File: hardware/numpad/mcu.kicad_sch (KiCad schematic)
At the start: 9 parts, among them J4 Conn_01x02_Female, J5 Conn_01x02_Male, U1 STM32L011F4Px

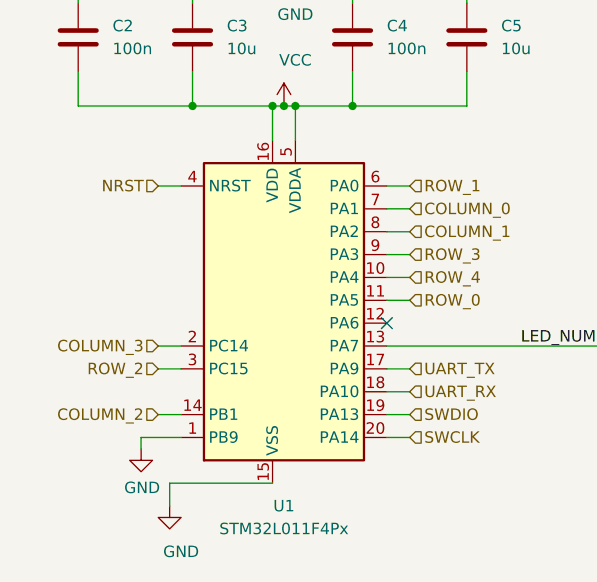
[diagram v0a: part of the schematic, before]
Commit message: Numpad: Exchange MCU for an available version
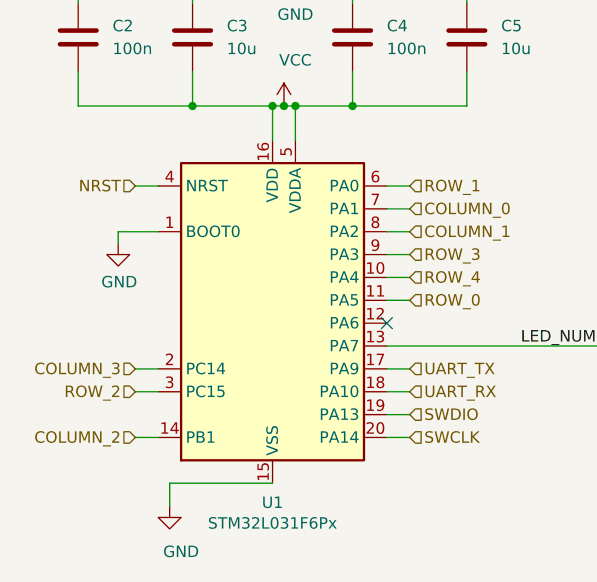
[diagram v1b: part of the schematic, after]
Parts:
- removed U1: STM32L011F4Px, Package_SO:TSSOP-20_4.4x6.5mm_P0.65mm, symbol MCU_ST_STM32L0:STM32L011F4Px
- added U1: STM32L031F6Px, Package_SO:TSSOP-20_4.4x6.5mm_P0.65mm, symbol MCU_ST_STM32L0:STM32L031F6Px
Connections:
- net COLUMN_0: now also U1.7 (PA1)
- net COLUMN_1: now also U1.8 (PA2)
- net COLUMN_2: now also U1.14 (PB1)
- net COLUMN_3: now also U1.2 (PC14)
- net GND: now also U1.1 (BOOT0), U1.15 (VSS)
- net LED_NUMLOCK: now also U1.13 (PA7)
- net NRST: now also U1.4 (NRST)
- net ROW_0: now also U1.11 (PA5)
- net ROW_1: now also U1.6 (PA0)
- net ROW_2: now also U1.3 (PC15)
- net ROW_3: now also U1.9 (PA3)
- net ROW_4: now also U1.10 (PA4)
- net SWCLK: now also U1.20 (PA14)
- net SWDIO: now also U1.19 (PA13)
- net UART_RX: now also U1.18 (PA10)
- net UART_TX: now also U1.17 (PA9)
- net VCC: now also U1.16 (VDD), U1.5 (VDDA)
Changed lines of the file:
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@@
     (stroke (width 0) (type solid) (color 0 0 0 0))
   )
-  (wire (pts (xy 86.995 118.11) (xy 91.44 118.11))
-    (stroke (width 0) (type solid) (color 0 0 0 0))
-  )
-  (wire (pts (xy 86.995 119.38) (xy 86.995 118.11))
-    (stroke (width 0) (type solid) (color 0 0 0 0))
-  )
-  (wire (pts (xy 88.9 90.17) (xy 91.44 90.17))
-    (stroke (width 0) (type solid) (color 0 0 0 0))
-  )
-  (wire (pts (xy 88.9 107.95) (xy 91.44 107.95))
-    (stroke (width 0) (type solid) (color 0 0 0 0))
-  )
-  (wire (pts (xy 88.9 110.49) (xy 91.44 110.49))
-    (stroke (width 0) (type solid) (color 0 0 0 0))
-  )
-  (wire (pts (xy 88.9 115.57) (xy 91.44 115.57))
+  (wire (pts (xy 84.455 95.25) (xy 88.9 95.25))
+    (stroke (width 0) (type solid) (color 0 0 0 0))
+  )
+  (wire (pts (xy 84.455 96.52) (xy 84.455 95.25))
+    (stroke (width 0) (type solid) (color 0 0 0 0))
+  )
+  (wire (pts (xy 86.36 90.17) (xy 88.9 90.17))
+    (stroke (width 0) (type solid) (color 0 0 0 0))
+  )
+  (wire (pts (xy 86.36 110.49) (xy 88.9 110.49))
+    (stroke (width 0) (type solid) (color 0 0 0 0))
+  )
+  (wire (pts (xy 86.36 113.03) (xy 88.9 113.03))
+    (stroke (width 0) (type solid) (color 0 0 0 0))
+  )
+  (wire (pts (xy 86.36 118.11) (xy 88.9 118.11))
     (stroke (width 0) (type solid) (color 0 0 0 0))
   )
@@
     (effects (font (size 1.27 1.27)) (justify left bottom))
   )
-  (hierarchical_label "NRST" (shape input) (at 88.9 90.17 180)
+  (hierarchical_label "NRST" (shape input) (at 86.36 90.17 180)
     (effects (font (size 1.27 1.27)) (justify right))
   )
-  (hierarchical_label "COLUMN_3" (shape input) (at 88.9 107.95 180)
+  (hierarchical_label "COLUMN_3" (shape input) (at 86.36 110.49 180)
     (effects (font (size 1.27 1.27)) (justify right))
   )
-  (hierarchical_label "ROW_2" (shape input) (at 88.9 110.49 180)
+  (hierarchical_label "ROW_2" (shape input) (at 86.36 113.03 180)
     (effects (font (size 1.27 1.27)) (justify right))
   )
-  (hierarchical_label "COLUMN_2" (shape input) (at 88.9 115.57 180)
+  (hierarchical_label "COLUMN_2" (shape input) (at 86.36 118.11 180)
     (effects (font (size 1.27 1.27)) (justify right))
   )
@@
     (pin "1")
   )
-  (symbol (lib_id "power:GND") (at 86.995 119.38 0) (unit 1)
-    (in_bom yes) (on_board yes)
-    (property "Reference" "#PWR0116" (id 0) (at 86.995 125.73 0)
-      (effects (font (size 1.27 1.27)) hide)
-    )
-    (property "Value" "GND" (id 1) (at 87.1093 123.7044 0))
-    (property "Footprint" "" (id 2) (at 86.995 119.38 0)
-      (effects (font (size 1.27 1.27)) hide)
-    )
-    (property "Datasheet" "" (id 3) (at 86.995 119.38 0)
+  (symbol (lib_id "power:GND") (at 84.455 96.52 0) (unit 1)
+    (in_bom yes) (on_board yes)
+    (property "Reference" "#PWR0116" (id 0) (at 84.455 102.87 0)
+      (effects (font (size 1.27 1.27)) hide)
+    )
+    (property "Value" "GND" (id 1) (at 84.5693 100.8444 0))
+    (property "Footprint" "" (id 2) (at 84.455 96.52 0)
+      (effects (font (size 1.27 1.27)) hide)
+    )
+    (property "Datasheet" "" (id 3) (at 84.455 96.52 0)
       (effects (font (size 1.27 1.27)) hide)
     )
@@
     (pin "2")
   )
-  (symbol (lib_id "MCU_ST_STM32L0:STM32L011F4Px") (at 104.14 102.87 0) (unit 1)
-    (in_bom yes) (on_board yes)
-    (property "Reference" "U1" (id 0) (at 102.87 125.73 0))
-    (property "Value" "STM32L011F4Px" (id 1) (at 102.87 128.27 0))
-    (property "Footprint" "Package_SO:TSSOP-20_4.4x6.5mm_P0.65mm" (id 2) (at 93.98 120.65 0)
+  (symbol (lib_id "MCU_ST_STM32L0:STM32L031F6Px") (at 101.6 102.87 0) (unit 1)
+    (in_bom yes) (on_board yes)
+    (property "Reference" "U1" (id 0) (at 101.6 125.3554 0))
+    (property "Value" "STM32L031F6Px" (id 1) (at 101.6 127.6541 0))
+    (property "Footprint" "Package_SO:TSSOP-20_4.4x6.5mm_P0.65mm" (id 2) (at 91.44 120.65 0)
       (effects (font (size 1.27 1.27)) (justify right) hide)
     )
-    (property "Datasheet" "http://www.st.com/st-web-ui/static/active/en/resource/technical/document/datasheet/DM00206508.pdf" (id 3) (at 104.14 102.87 0)
-      (effects (font (size 1.27 1.27)) hide)
-    )
-    (property "Mouser" "511-STM32L011F4P6 " (id 4) (at 104.14 102.87 0)
-      (effects (font (size 1.27 1.27)) hide)
-    )
-    (property "Part Name" "STM32L011F4P6" (id 5) (at 104.14 102.87 0)
-      (effects (font (size 1.27 1.27)) hide)
-    )
+    (property "Datasheet" "http://www.st.com/st-web-ui/static/active/en/resource/technical/document/datasheet/DM00140359.pdf" (id 3) (at 101.6 102.87 0)
+      (effects (font (size 1.27 1.27)) hide)
+    )
+    (property "Mouser" "511-STM32L031F6P7" (id 4) (at 101.6 102.87 0)
+      (effects (font (size 1.27 1.27)) hide)
+    )
+    (property "Part Name" "STM32L031F6P7" (id 5) (at 101.6 102.87 0)
+      (effects (font (size 1.27 1.27)) hide)
+    )
+    (pin "1")
     (pin "4")
     (pin "6")
@@
     (pin "17")
     (pin "14")
-    (pin "1")
     (pin "2")
     (pin "3")

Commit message: Main & Numpad: Exchange unavailable capacitors
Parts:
- C2, C4: Mouser 581-06033C104KAT4A -> 581-0603YC104MAT4A; Part Name AVX 06033C104KAT4A -> AVX 0603YC104MAT4A
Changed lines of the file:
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@@
       (effects (font (size 1.27 1.27)) hide)
     )
-    (property "Mouser" "581-06033C104KAT4A" (id 4) (at 80.01 73.66 0)
+    (property "Mouser" "581-0603YC104MAT4A " (id 4) (at 80.01 73.66 0)
       (effects (font (size 1.27 1.27)) hide)
     )
-    (property "Part Name" "AVX 06033C104KAT4A " (id 5) (at 80.01 73.66 0)
+    (property "Part Name" "AVX 0603YC104MAT4A" (id 5) (at 80.01 73.66 0)
       (effects (font (size 1.27 1.27)) hide)
     )
@@
       (effects (font (size 1.27 1.27)) hide)
     )
-    (property "Mouser" "581-06033C104KAT4A" (id 4) (at 110.49 73.66 0)
+    (property "Mouser" "581-0603YC104MAT4A " (id 4) (at 110.49 73.66 0)
       (effects (font (size 1.27 1.27)) hide)
     )
-    (property "Part Name" "AVX 06033C104KAT4A " (id 5) (at 110.49 73.66 0)
+    (property "Part Name" "AVX 0603YC104MAT4A" (id 5) (at 110.49 73.66 0)
       (effects (font (size 1.27 1.27)) hide)
     )
